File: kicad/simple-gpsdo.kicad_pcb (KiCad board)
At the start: 2 copper layers, 119.5 x 74.5 mm, 103 parts, among them J1 PPS_OUT, J2 PWR, J3 ISP, J4 GPS_NEO, J5 GPS_IN, J6 10MHz_OUT, J7 NEO-6M, J8 10MHz_OUT, J9 USB_C, Q1 DMP3099L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

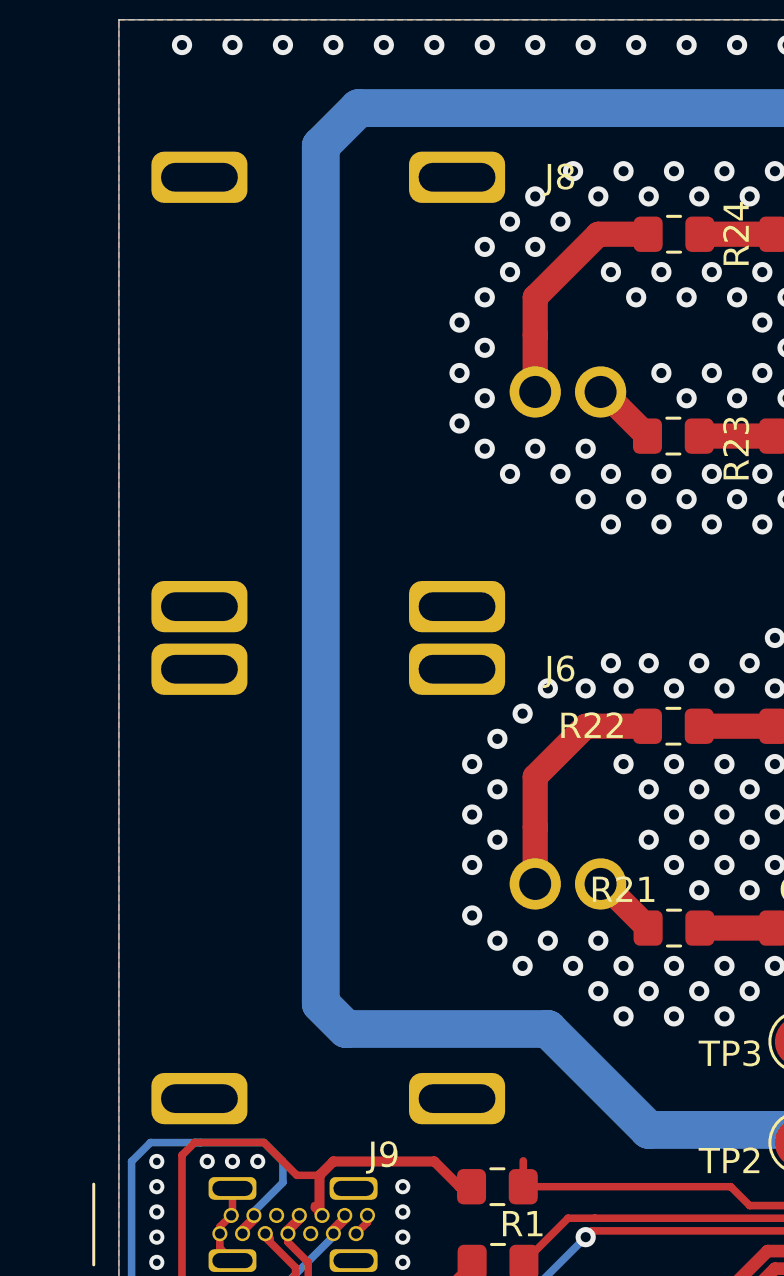
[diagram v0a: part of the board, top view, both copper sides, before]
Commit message: updated pictures, moved BNC jacks slightly inward
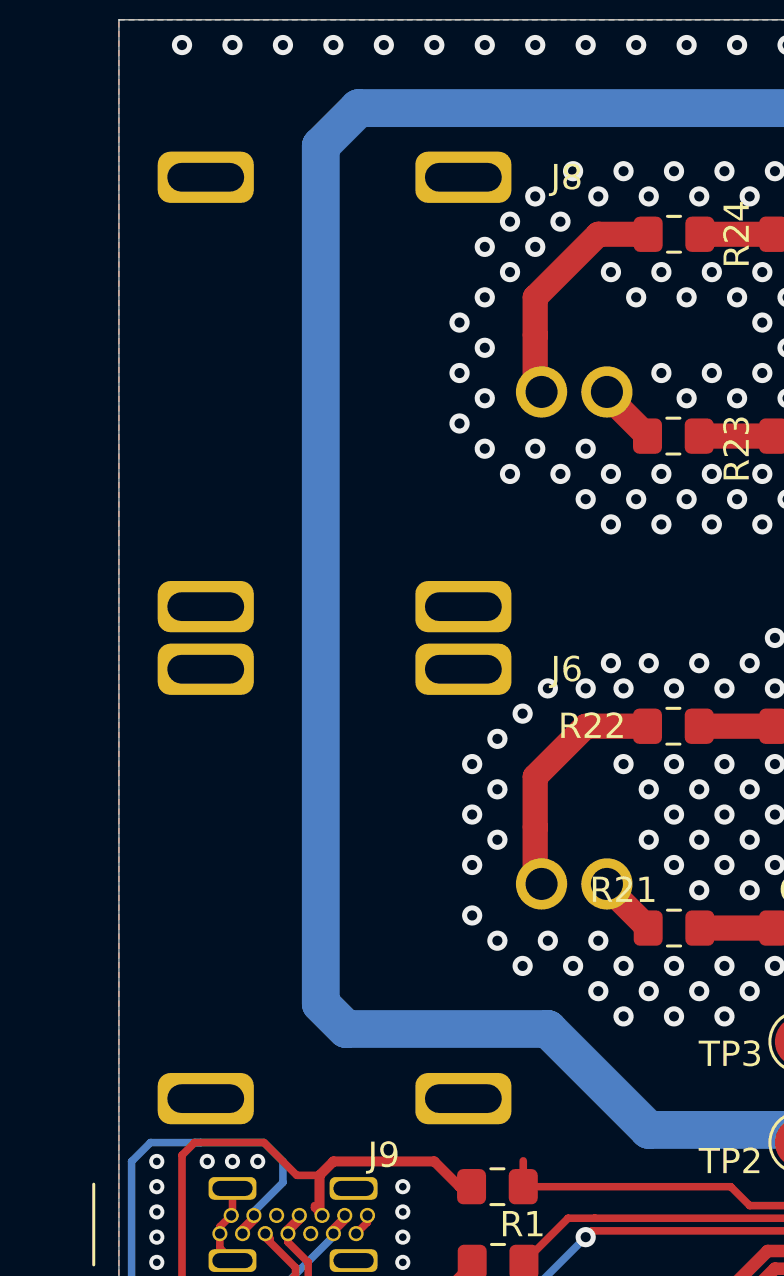
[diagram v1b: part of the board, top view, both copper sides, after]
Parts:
- moved J6 0.25 mm to (91.8, 109.2)
- moved J8 0.25 mm to (91.8, 89.8)

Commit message: schematic cleanup and re-plot of gerber files
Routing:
- net Net-(J9-PadA7): track 28.6 -> 28.1 mm
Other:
- rule via_min_size: 0.45 -> 0.6

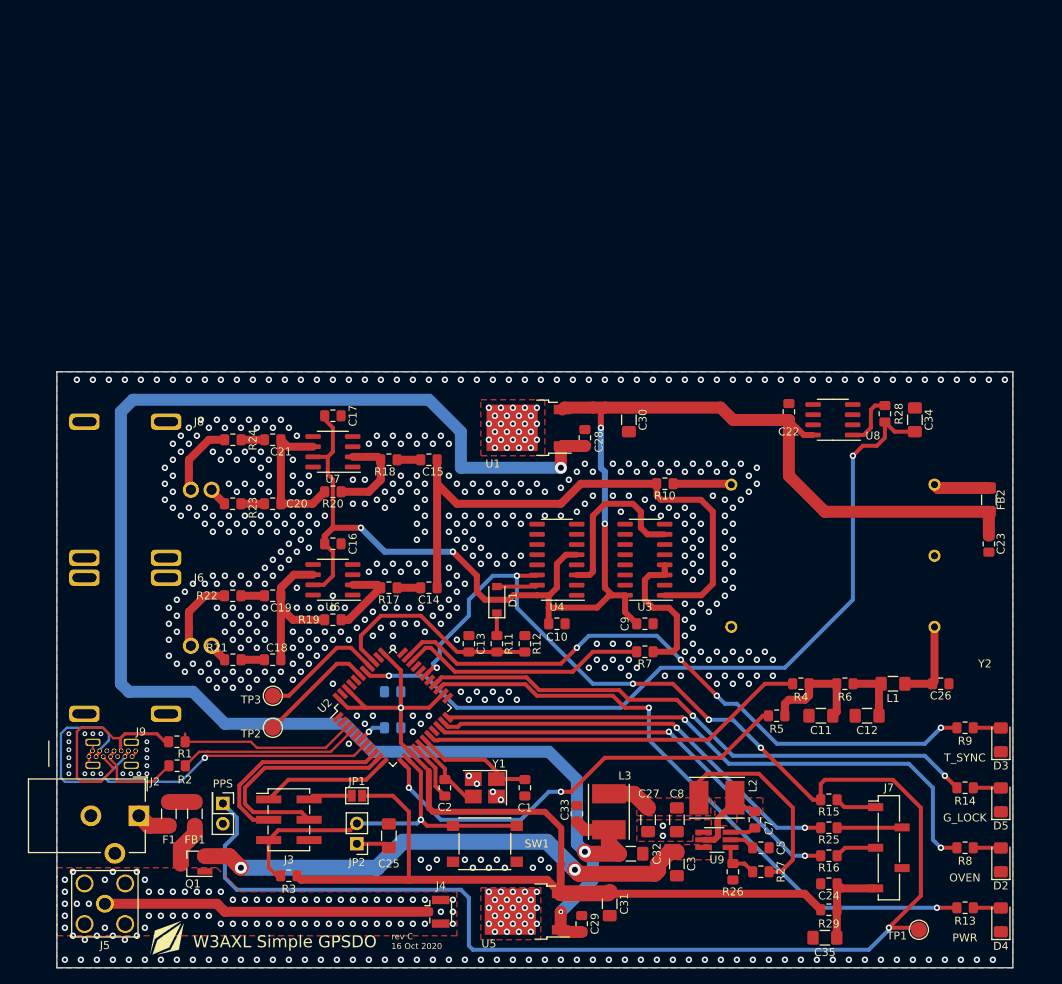
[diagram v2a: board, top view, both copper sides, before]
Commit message: finalized simple schematic, started PCB rework
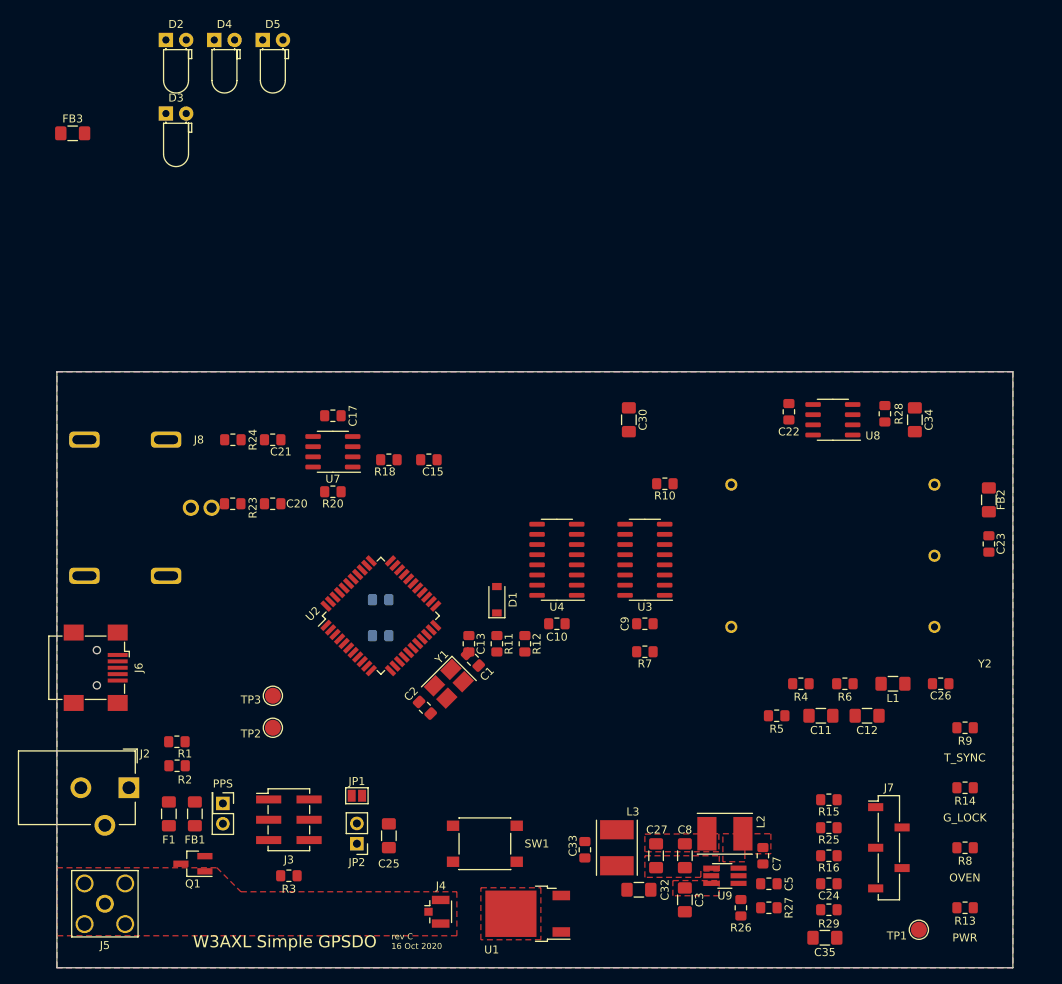
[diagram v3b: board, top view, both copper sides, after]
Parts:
- removed C14, C16, C18, C19: 0.1uF, Capacitor_SMD:C_0805_2012Metric_Pad1.15x1.40mm_HandSolder
- removed C28, C29: 1uF, Capacitor_SMD:C_0805_2012Metric_Pad1.15x1.40mm_HandSolder
- removed C31: 4.7uF, Capacitor_SMD:C_1206_3216Metric_Pad1.42x1.75mm_HandSolder
- removed G***: LOGO, w3axl-logos:logo-4.2x4.2
- removed J9: USB_C, Kycon:KUSBX-SL-CS1N14-B
- removed R17, R19: 10k, Resistor_SMD:R_0805_2012Metric_Pad1.15x1.40mm_HandSolder
- removed R21, R22: 50R, Resistor_SMD:R_0805_2012Metric_Pad1.15x1.40mm_HandSolder
- removed U5: BD50FC0FP-E2, Package_TO_SOT_SMD:TO-252-2
- removed U6: LM7171, Package_SO:SOIC-8_3.9x4.9mm_P1.27mm
- added FB3: Ferrite, Fuse:Fuse_1206_3216Metric_Pad1.42x1.75mm_HandSolder, F.Cu at (77.0, 45.2)
- D2, D3, D4, D5: footprint LED_SMD:LED_1206_3216Metric_Pad1.42x1.75mm_HandSolder -> LED_THT:LED_D3.0mm_Horizontal_O1.27mm_Z2.0mm_Clear
- J6: value 10MHz_OUT -> USB_B_Micro; footprint molex:734152980 -> Connector_USB:USB_Mini-B_Wuerth_65100516121_Horizontal
- U9: value AP62301WU-7 -> AP62150WU-7
- moved D4 147.5 mm to (94.7, 33.5), turned to 0 degrees
- moved D2 146.3 mm to (88.6, 33.5), turned to 0 degrees
- moved D5 132.4 mm to (100.7, 33.5), turned to 0 degrees
- moved D3 130.5 mm to (88.6, 42.7), turned to 0 degrees
- moved U1 60.8 mm to (133.8, 142.8)
- moved C1 17.3 mm to (127.0, 111.0), turned to 135 degrees
- moved Y1 13.8 mm to (124.0, 114.0), turned to 225 degrees
- moved J6 12.1 mm to (80.0, 112.0)
- moved C4 11.6 mm to (115.5, 108.0)
- moved C6 11.6 mm to (115.5, 103.5)
- moved U2 11.6 mm to (115.5, 105.5)
- moved C2 10.3 mm to (121.0, 117.0), turned to 315 degrees
- moved C27 4.61 mm to (149.9, 135.5)
- moved C3 4.61 mm to (153.5, 141.0)
- moved C32 4.61 mm to (147.8, 139.8)
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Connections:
- C10 pad 2: +5VA -> +5V
- C17 pad 2: +5VA -> +5V
- C22 pad 2: +5VA -> +5V
- C23 pad 2: +5VA -> +5V
- C30 pad 1: +5VA -> +5V
- C6 pad 2: +5VD -> +5V
- C9 pad 2: +5VA -> +5V
- FB2 pad 1: +5VA -> +5V
- J6 pad 3: GND -> Net-(J6-Pad3)
- JP1 pad 2: +5VD -> +5V
- L1 pad 1: Net-(C26-Pad2) -> OSC_CTRL
- L1 pad 2: OSC_CTRL -> Net-(C26-Pad2)
- R1 pad 2: Net-(J9-PadA7) -> Net-(J6-Pad2)
- R2 pad 1: Net-(J9-PadA6) -> Net-(J6-Pad3)
- R29 pad 1: +5VD -> +5V
- R3 pad 1: +5VD -> +5V
- U1 pad 3: +5VA -> +5V
- U2 pad 14: +5VD -> +5V
- U2 pad 24: +5VD -> +5V
- U2 pad 34: +5VD -> +5V
- U2 pad 42: +5VD -> +5V
- U2 pad 44: +5VD -> +5V
- U3 pad 16: +5VA -> +5V
- U4 pad 16: +5VA -> +5V
- U4 pad 5: +5VA -> +5V
- U7 pad 7: +5VA -> +5V
- U8 pad 8: +5VA -> +5V
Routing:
- net GPS_PPS: track 213.0 -> 0.00 mm, vias 6 -> 0
- net +6V: track 199.6 -> 0.00 mm, vias 3 -> 0
- net +5VA: track 178.0 -> 0.00 mm, vias 4 -> 0
- net +5VD: track 149.7 -> 0.00 mm, vias 1 -> 0
- net /ADC2: track 97.6 -> 0.00 mm, vias 2 -> 0
- net POWER_OK: track 78.9 -> 0.00 mm, vias 2 -> 0
- net TIME_LOCK: track 78.5 -> 0.00 mm, vias 4 -> 0
- net OVEN_TEMP: track 74.2 -> 0.00 mm, vias 2 -> 0
- net GPS_LOCK: track 72.4 -> 0.00 mm, vias 2 -> 0
- net 10MHz: track 71.0 -> 0.00 mm
- net Net-(C3-Pad1): track 64.2 -> 0.00 mm, vias 2 -> 0
- net Net-(FB3-Pad2): track 61.1 -> 0.00 mm, vias 1 -> 0
- net /PWM_D11: track 55.9 -> 0.00 mm, vias 2 -> 0
- net GPS_TX: track 54.5 -> 0.00 mm, vias 2 -> 0
- net GPS_RX: track 53.0 -> 0.00 mm, vias 2 -> 0
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
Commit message: more PCB work
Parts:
- moved D4 147.6 mm to (192.0, 144.5), turned to 90 degrees
- moved D2 146.3 mm to (192.0, 137.0), turned to 90 degrees
- moved D5 132.4 mm to (192.0, 129.5), turned to 90 degrees
- moved D3 130.3 mm to (192.0, 122.0), turned to 90 degrees
- moved FB3 69.2 mm to (95.0, 112.0), turned to 270 degrees
- moved C30 56.3 mm to (137.0, 136.5), turned to 180 degrees
- moved TP1 23.9 mm to (171.2, 123.8)
- moved TP3 19.7 mm to (106.2, 96.2)
- moved TP2 19.5 mm to (102.5, 100.0)
- moved R7 17.7 mm to (131.2, 106.2)
- moved C13 15.3 mm to (126.2, 93.8), turned to 180 degrees
- moved R11 12.1 mm to (126.2, 97.5), turned to 180 degrees
- moved R2 10.8 mm to (90.0, 113.5)
- moved R1 10.8 mm to (90.0, 110.5)
- moved R12 10.6 mm to (126.2, 101.2), turned to 0 degrees
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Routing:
- net GND: vias 0 -> 27
- removed copper zone on F.Cu, net Net-(C27-Pad1)
- removed copper zone on F.Cu, net Net-(C3-Pad1)
- removed copper zone on F.Cu, net Net-(C7-Pad2)

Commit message: finalized new schematic and board
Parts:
- removed J4: GPS_NEO, Connector_Coaxial:U.FL_Hirose_U.FL-R-SMT-1_Vertical
- removed J5: GPS_IN, Connector_Coaxial:SMA_Amphenol_132203-12_Horizontal
- added D6: PPS, LED_THT:LED_D3.0mm_Horizontal_O1.27mm_Z2.0mm_Clear, F.Cu at (191.5, 115.0)
- added G***: LOGO, w3axl-logos:logo-4.2x4.2, F.Cu at (94.2, 102.5)
- added R17: 470, Resistor_SMD:R_0805_2012Metric_Pad1.15x1.40mm_HandSolder, F.Cu at (188.0, 112.5)
- SW1: footprint Button_Switch_SMD:SW_SPST_PTS645 -> Connector_PinHeader_2.54mm:PinHeader_1x02_P2.54mm_Vertical
- moved R27 64.3 mm to (101.5, 142.5), turned to 270 degrees
- moved R26 61.8 mm to (100.5, 139.0), turned to 180 degrees
- moved C5 61.1 mm to (104.8, 142.5), turned to 90 degrees
- moved C7 57.1 mm to (108.4, 142.1), turned to 0 degrees
- moved U9 55.5 mm to (104.8, 136.8), turned to 270 degrees
- moved C3 54.5 mm to (101.2, 132.8), turned to 90 degrees
- moved L2 50.2 mm to (110.2, 136.8), turned to 90 degrees
- moved C27 45.5 mm to (106.2, 131.2), turned to 180 degrees
- moved C8 42.9 mm to (112.5, 131.2), turned to 0 degrees
- moved L3 30.1 mm to (116.8, 136.8), turned to 90 degrees
- moved TP3 30.0 mm to (133.5, 108.8)
- moved TP2 27.7 mm to (128.8, 108.8)
- moved C32 26.3 mm to (123.2, 137.5)
- moved R3 24.7 mm to (127.5, 130.5), turned to 90 degrees
- moved C6 24.3 mm to (135.0, 118.0)
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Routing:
- net +5V: track 0.00 -> 287.7 mm, vias 0 -> 6
- net GPS_PPS: track 0.00 -> 160.2 mm, vias 0 -> 4
- net /ADC2: track 0.00 -> 103.6 mm, vias 0 -> 2
- net POWER_OK: track 0.00 -> 62.5 mm
- net Net-(R2-Pad2): track 0.00 -> 59.9 mm
- net Net-(R1-Pad1): track 0.00 -> 59.4 mm
- net /PWM_D11: track 0.00 -> 56.6 mm, vias 0 -> 2
- net Net-(FB3-Pad2): track 0.00 -> 56.4 mm
- net OVEN_TEMP: track 0.00 -> 53.3 mm
- net GPS_LOCK: track 0.00 -> 51.8 mm
- net TIME_LOCK: track 0.00 -> 47.6 mm
- net /PWM_D3: track 0.00 -> 38.8 mm, vias 0 -> 2
- net GPS_TX: track 0.00 -> 38.0 mm
- net GPS_RX: track 0.00 -> 35.7 mm
- net ~RST: track 0.00 -> 33.7 mm
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- added copper zone on F.Cu, net Net-(C27-Pad1)
- added copper zone on F.Cu, net Net-(C3-Pad1)
- added copper zone on F.Cu, net Net-(C7-Pad1)
- added copper zone on F.Cu, net Net-(C7-Pad2)
- added copper zone on F.Cu, net Net-(R26-Pad1)
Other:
- rule pad_to_mask_clearance: 0.05 -> 0
- board text added: "GPSLCK"
- board text added: "TIMESYNC"
- board text added: "rev D 22 Oct 2020"
- board text removed: "G_LOCK"
- board text removed: "T_SYNC"
- board text removed: "rev C 16 Oct 2020"

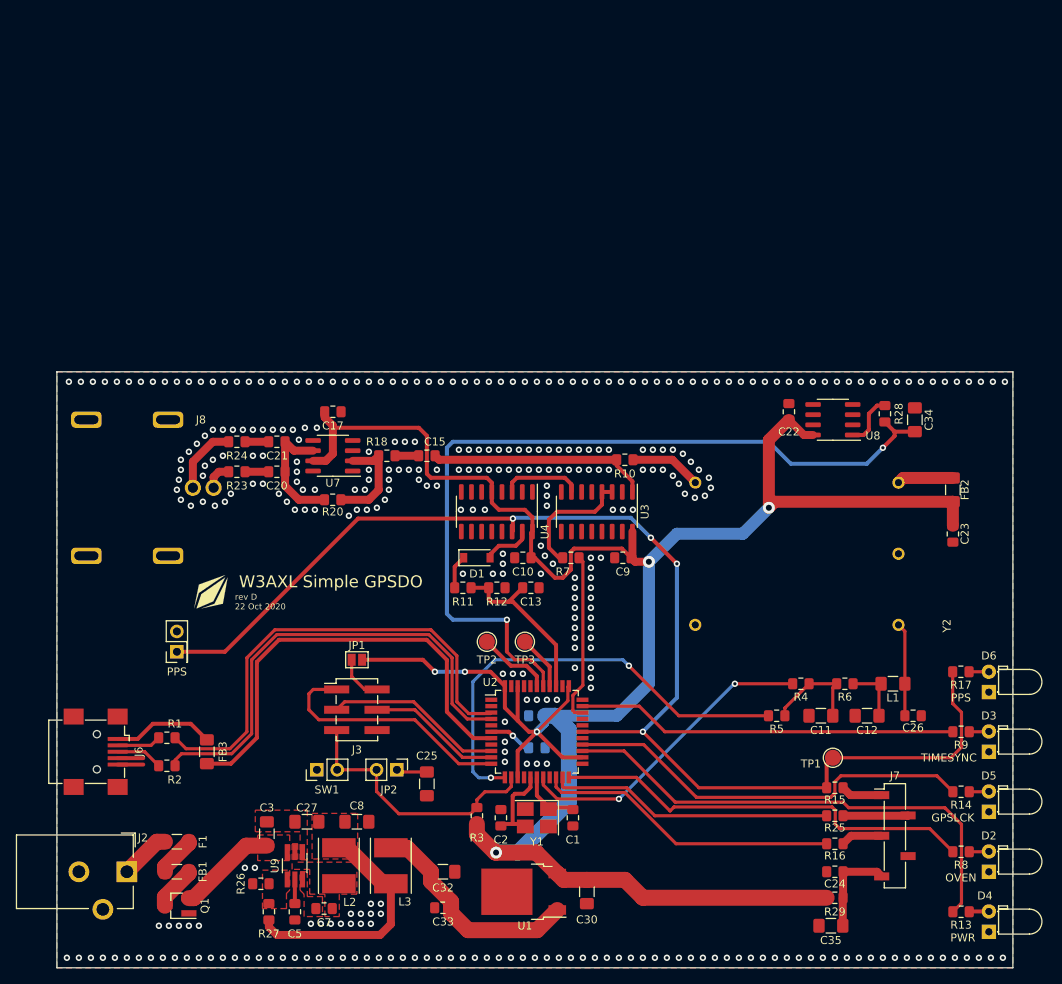
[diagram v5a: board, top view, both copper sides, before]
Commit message: Updated tantalum footprints, started new BOM
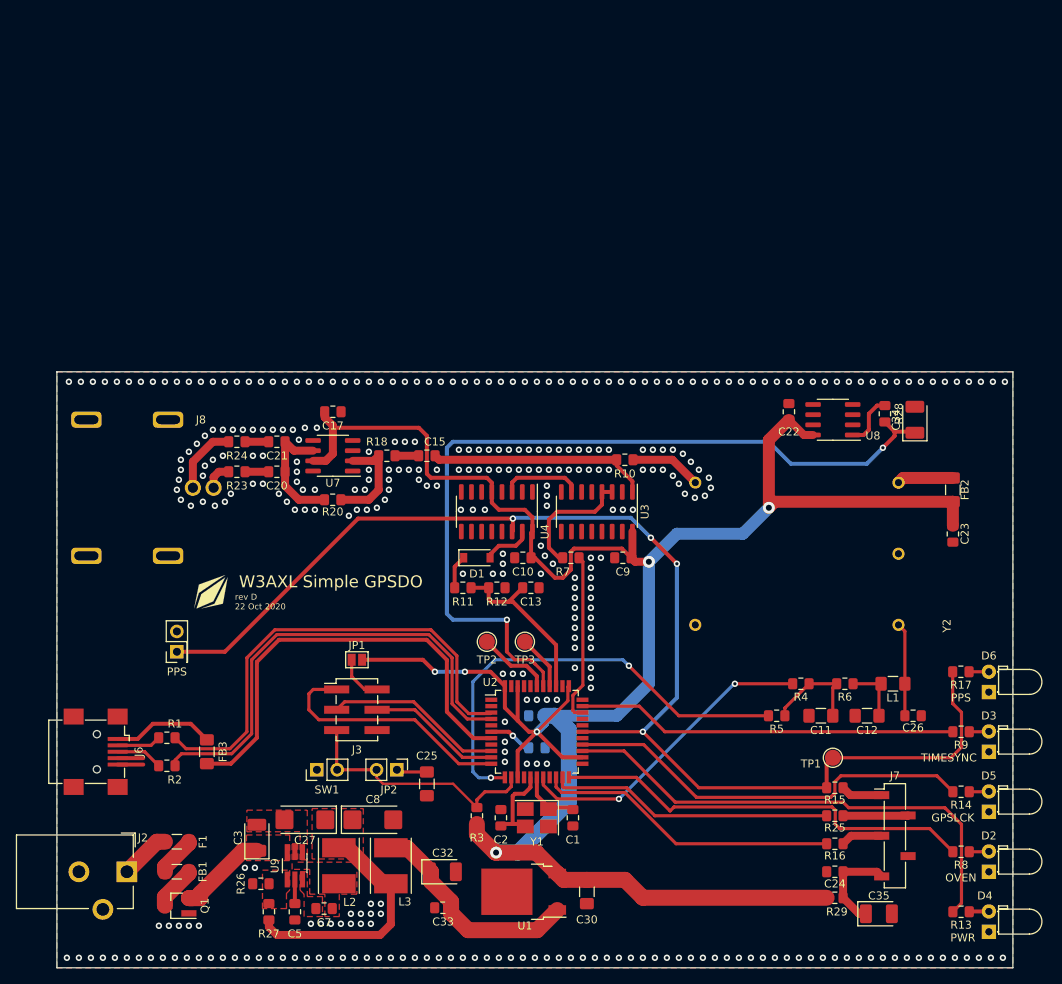
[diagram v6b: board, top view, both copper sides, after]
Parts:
- C27, C8: footprint Capacitor_SMD:C_1206_3216Metric_Pad1.42x1.75mm_HandSolder -> Capacitor_Tantalum_SMD:CP_EIA-6032-20_AVX-F_Pad2.25x2.35mm_HandSolder
- C3, C32, C34, C35: footprint Capacitor_SMD:C_1206_3216Metric_Pad1.42x1.75mm_HandSolder -> Capacitor_Tantalum_SMD:CP_EIA-3528-15_AVX-H_Pad1.50x2.35mm_HandSolder
- moved C35 6.18 mm to (177.8, 142.8), turned to 0 degrees
- moved C8 2.02 mm to (114.5, 131.0)
- moved C3 1.35 mm to (100.0, 133.2)
- moved C27 0.35 mm to (106.0, 131.0)
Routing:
- net ~RST: track 33.7 -> 32.1 mm
- net Net-(C3-Pad1): track 12.5 -> 11.9 mm
